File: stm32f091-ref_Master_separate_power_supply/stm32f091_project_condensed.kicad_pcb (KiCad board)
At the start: 2 copper layers, 83.8 x 130.8 mm, 62 parts, among them J1 Conn_02x05_Odd_Even, J2 Conn_01x08_Female, J3 Conn_01x02_Female, J4 Conn_01x09_Female, SW1 SW_Push, U1 LD1117S33TR_SOT223, U2 LM324, U3 STM32F091RCTx, U4 LM386

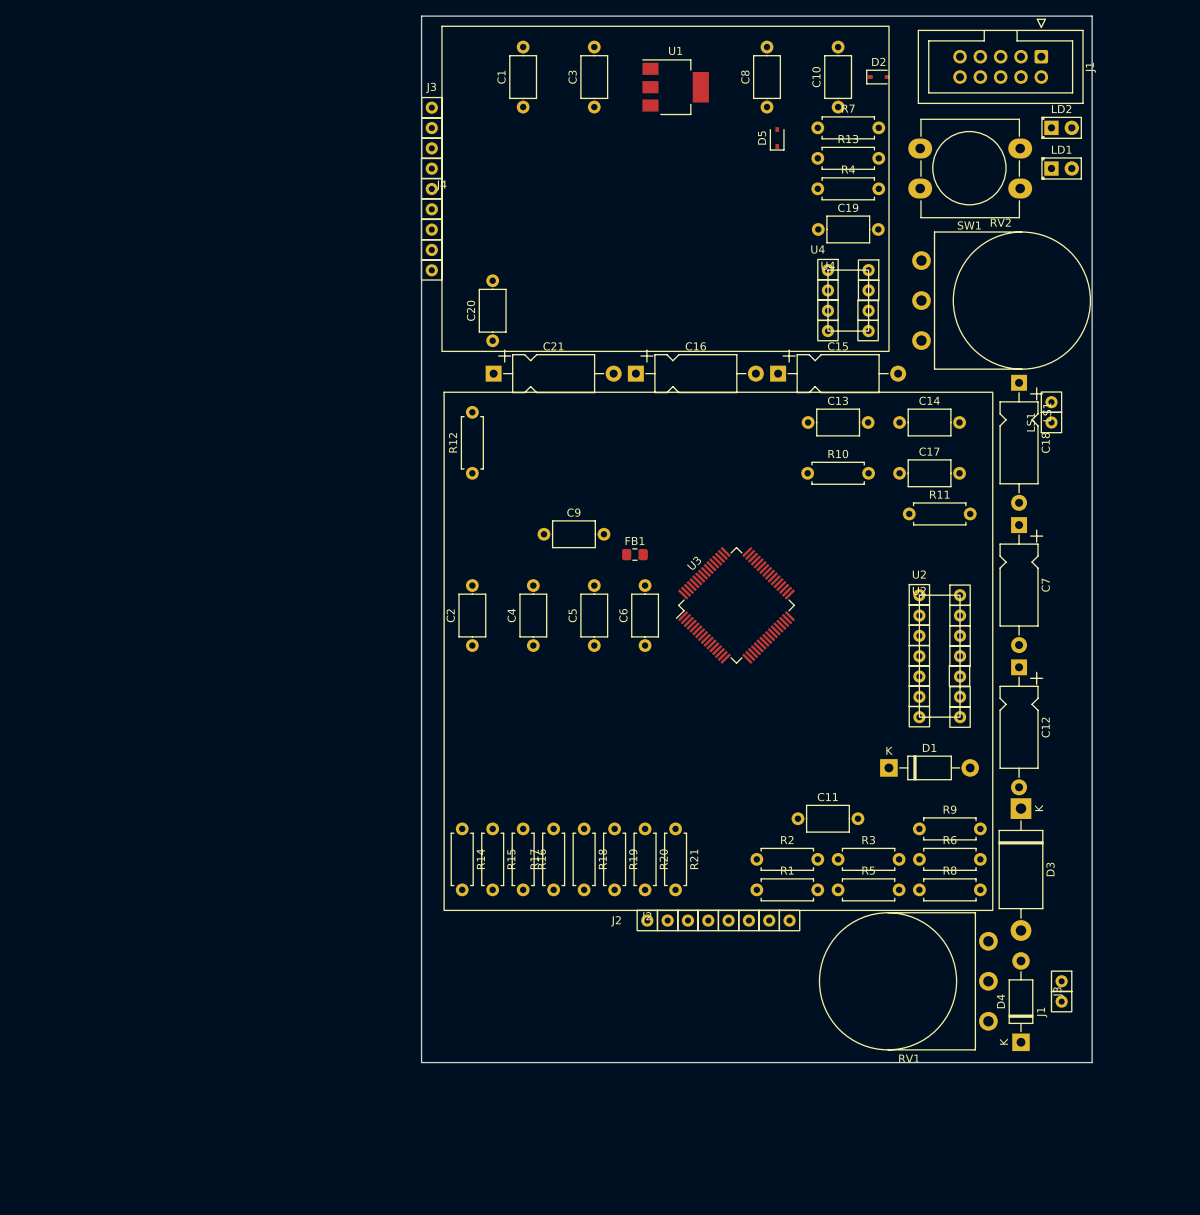
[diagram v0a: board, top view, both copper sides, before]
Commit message: PCB designs w/out traces for a regular and condensed PCB
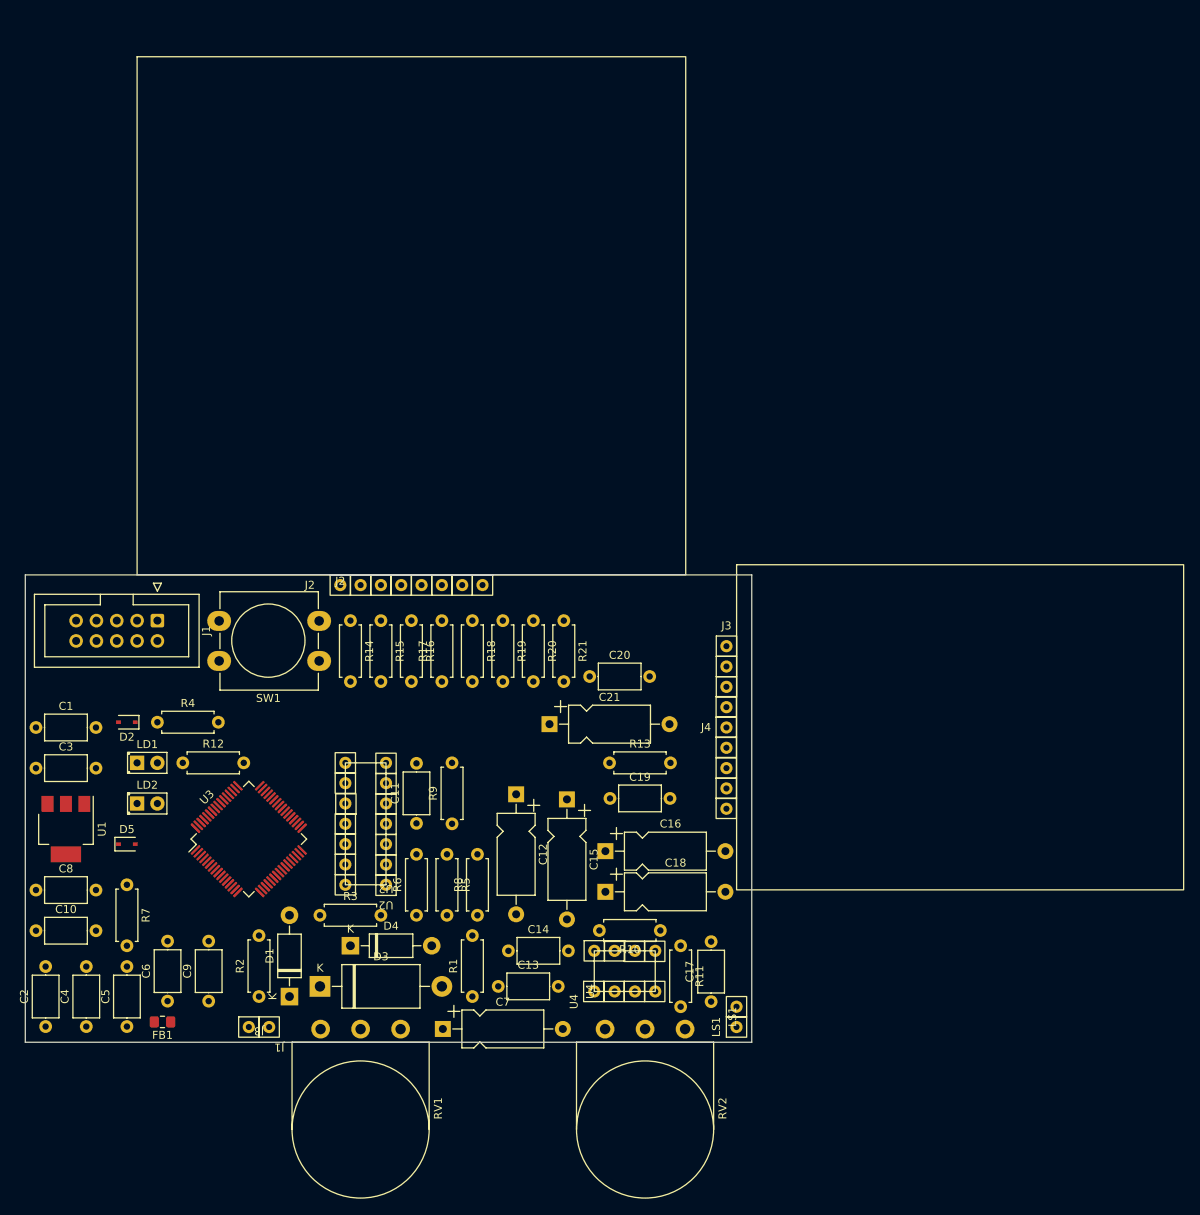
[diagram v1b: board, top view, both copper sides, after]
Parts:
- moved C10 143.7 mm to (42.0, 135.8), turned to 0 degrees
- moved LD2 142.1 mm to (54.6, 119.9)
- moved LD1 136.3 mm to (54.6, 114.9)
- moved C8 133.9 mm to (42.0, 130.8), turned to 0 degrees
- moved J1 131.1 mm to (57.2, 97.1)
- moved R7 128.1 mm to (53.4, 130.1), turned to -90 degrees
- moved D2 123.8 mm to (53.4, 109.8), turned to 180 degrees
- moved U1 120.0 mm to (45.7, 123.1), turned to -90 degrees
- moved D5 120.0 mm to (53.4, 125.0), turned to 0 degrees
- moved C3 108.2 mm to (42.0, 115.5), turned to 0 degrees
- moved R4 106.1 mm to (57.2, 109.8)
- moved SW1 105.7 mm to (77.4, 102.1)
- moved J3 100.4 mm to (69.9, 147.9), turned to 180 degrees
- moved C1 98.6 mm to (42.0, 110.4), turned to 0 degrees
- moved C7 95.7 mm to (92.8, 148.1), turned to 0 degrees
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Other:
- board size 83.8 x 130.8 mm -> 90.8 x 58.4 mm
- copper layers 2 -> 4
- rule pad_to_mask_clearance: 0.0508 -> 0.05
- board text added: "PillCB - Team 16 (4/13/2022 - V01) Jaideep Damle, Lauren Gunter, Nidhi Kunigal, Elizabeth McNaughton"

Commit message: changed r's and c's to SM in condensed PCB design
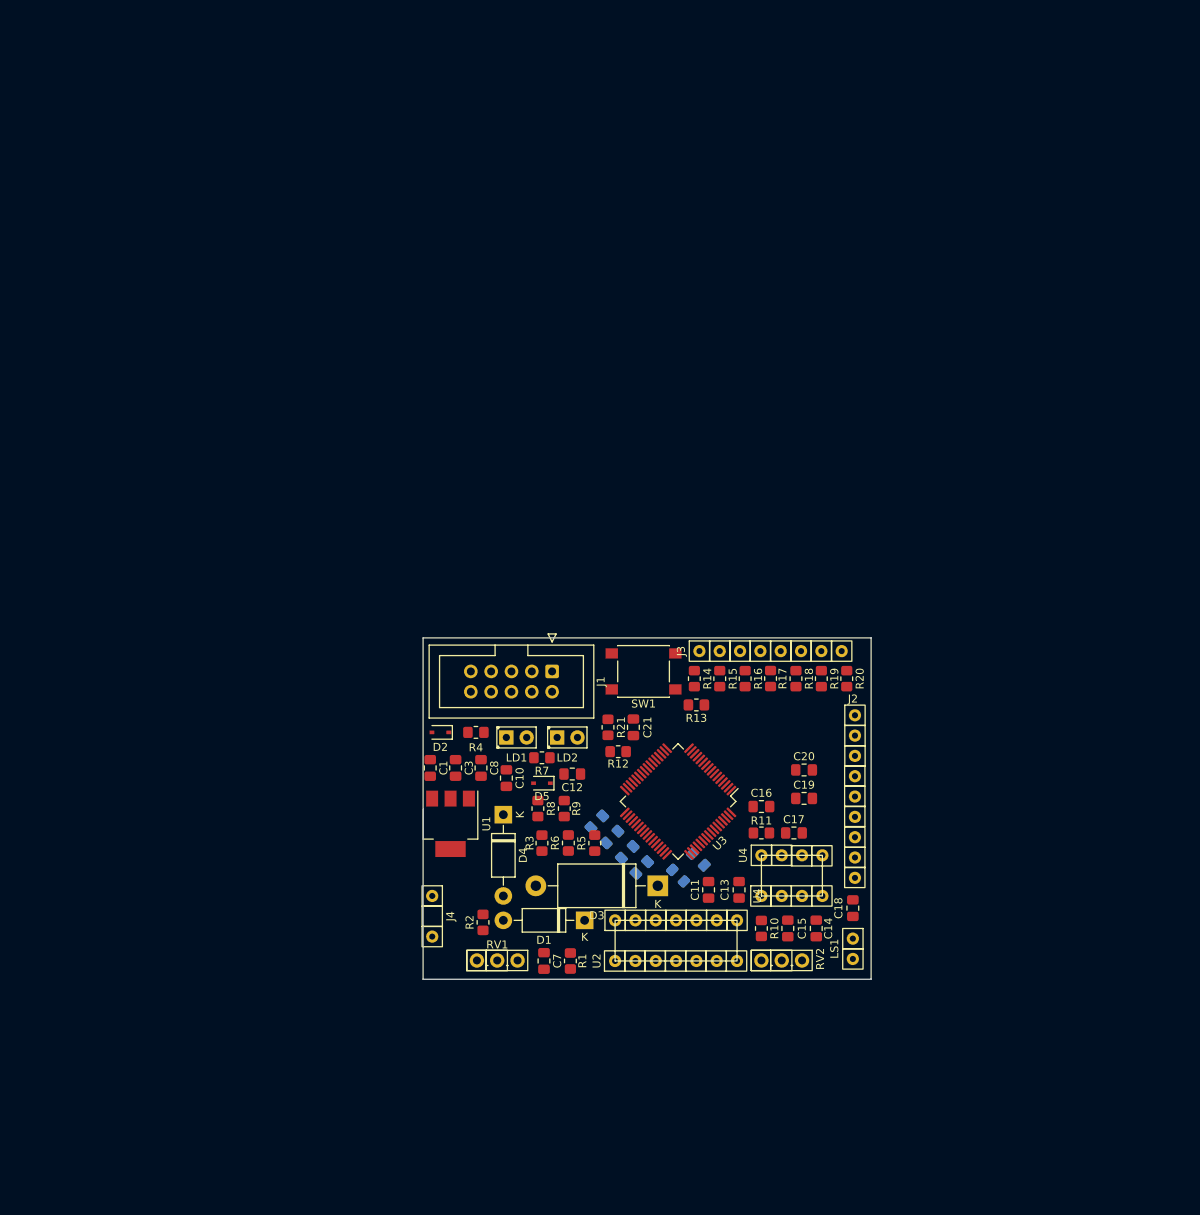
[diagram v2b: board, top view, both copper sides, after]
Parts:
- C1, C10, C11, C13, C14, C17, C19, C3, C8: footprint Capacitor_THT:C_Axial_L5.1mm_D3.1mm_P7.50mm_Horizontal -> Capacitor_SMD:C_0805_2012Metric_Pad1.18x1.45mm_HandSolder
- C12, C15, C16, C18, C7: footprint Capacitor_THT:CP_Axial_L10.0mm_D4.5mm_P15.00mm_Horizontal -> Capacitor_SMD:C_0805_2012Metric_Pad1.18x1.45mm_HandSolder
- C2, C4, C5, C6, C9: footprint Capacitor_THT:C_Axial_L5.1mm_D3.1mm_P7.50mm_Horizontal -> Capacitor_SMD:C_0805_2012Metric_Pad1.18x1.45mm_HandSolder; moved to B.Cu
- C20: value .1uF -> 10uF; footprint Capacitor_THT:C_Axial_L5.1mm_D3.1mm_P7.50mm_Horizontal -> Capacitor_SMD:C_0805_2012Metric_Pad1.18x1.45mm_HandSolder
- C21: value 10uF -> .1uF; footprint Capacitor_THT:CP_Axial_L10.0mm_D4.5mm_P15.00mm_Horizontal -> Capacitor_SMD:C_0805_2012Metric_Pad1.18x1.45mm_HandSolder
- FB1: moved to B.Cu
- J2: value Conn_01x08_Female -> Conn_01x09_Female; footprint local_models:J2 -> local_models:J3
- J3: value Conn_01x02_Female -> Conn_01x08_Female; footprint local_models:J1 -> local_models:J2
- J4: value Conn_01x09_Female -> Conn_01x02_Female; footprint local_models:J3 -> local_models:J1
- R1, R10, R11, R12, R14, R15, R16, R17, R18, R19, R2, R20, R3, R4, R5, R6, R7, R8, R9: footprint Resistor_THT:R_Axial_DIN0207_L6.3mm_D2.5mm_P7.62mm_Horizontal -> Resistor_SMD:R_0805_2012Metric_Pad1.20x1.40mm_HandSolder
- R13: value 100K -> 1K; footprint Resistor_THT:R_Axial_DIN0207_L6.3mm_D2.5mm_P7.62mm_Horizontal -> Resistor_SMD:R_0805_2012Metric_Pad1.20x1.40mm_HandSolder
- R21: value 1K -> 100K; footprint Resistor_THT:R_Axial_DIN0207_L6.3mm_D2.5mm_P7.62mm_Horizontal -> Resistor_SMD:R_0805_2012Metric_Pad1.20x1.40mm_HandSolder
- RV1, RV2: footprint Potentiometer_THT:Potentiometer_Omeg_PC16BU_Vertical -> local_models:potentiometer
- SW1: footprint Button_Switch_THT:SW_PUSH-12mm_Wuerth-430476085716 -> Button_Switch_SMD:SW_SPST_PTS645
- moved J3 79.4 mm to (133.8, 100.9), turned to 0 degrees
- moved C2 73.5 mm to (112.1, 122.2), turned to 45 degrees
- moved C4 69.9 mm to (114.0, 124.1), turned to 45 degrees
- moved FB1 67.0 mm to (122.3, 129.0), turned to 135 degrees
- moved C5 66.2 mm to (115.9, 126.0), turned to 45 degrees
- moved C9 63.7 mm to (124.8, 126.9), turned to 135 degrees
- moved J2 62.6 mm to (145.6, 119.1)
- moved C10 61.8 mm to (100.8, 116.8), turned to -90 degrees
- moved C6 61.6 mm to (117.7, 127.9), turned to 45 degrees
- moved C8 57.7 mm to (97.6, 115.5), turned to -90 degrees
- moved R12 54.4 mm to (114.8, 113.5)
- moved R7 54.3 mm to (105.2, 114.2), turned to 180 degrees
- moved U3 53.9 mm to (122.3, 119.7), turned to -135 degrees
- moved LD2 53.2 mm to (107.1, 111.7)
- moved C3 52.5 mm to (94.4, 115.5), turned to -90 degrees
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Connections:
- C19 pad 1: /NRST -> +3V0
- C21 pad 1: +3V0 -> /NRST
- J2 pad 1: Net-(J2-Pad1) -> +3V0
- J2 pad 2: Net-(J2-Pad2) -> GND
- J2 pad 3: Net-(J2-Pad3) -> PB8
- J2 pad 4: Net-(J2-Pad4) -> PB11
- J2 pad 5: Net-(J2-Pad5) -> PB14
- J2 pad 6: Net-(J2-Pad6) -> PB5
- J2 pad 7: Net-(J2-Pad7) -> PB3
- J2 pad 8: Net-(J2-Pad8) -> +3V0
- J3 pad 1: /AC_SIGNAL -> Net-(J3-Pad1)
- J3 pad 2: GND -> Net-(J3-Pad2)
- J4 pad 1: +3V0 -> /AC_SIGNAL
- R13 pad 1: +3V0 -> /PC7
- R13 pad 2: /NRST -> Net-(J3-Pad1)
- R14 pad 1: /PC7 -> /PC6
- R14 pad 2: Net-(J2-Pad1) -> Net-(J3-Pad2)
- R15 pad 1: /PC6 -> /PC5
- R15 pad 2: Net-(J2-Pad2) -> Net-(J3-Pad3)
- R16 pad 1: /PC5 -> /PC4
- R16 pad 2: Net-(J2-Pad3) -> Net-(J3-Pad4)
- R17 pad 1: /PC4 -> /PC3
- R17 pad 2: Net-(J2-Pad4) -> Net-(J3-Pad5)
- R18 pad 1: /PC3 -> /PC2
- R18 pad 2: Net-(J2-Pad5) -> Net-(J3-Pad6)
- R19 pad 1: /PC2 -> /PC1
- R19 pad 2: Net-(J2-Pad6) -> Net-(J3-Pad7)
- R20 pad 1: /PC1 -> /PC0
- R20 pad 2: Net-(J2-Pad7) -> Net-(J3-Pad8)
- R21 pad 1: /PC0 -> +3V0
- R21 pad 2: Net-(J2-Pad8) -> /NRST
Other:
- board size 90.8 x 58.4 mm -> 56 x 42.7 mm
